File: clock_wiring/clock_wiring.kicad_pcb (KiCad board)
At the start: 2 copper layers, 142.2 x 142.2 mm, 38 parts, among them J1 Conn_01x01_Female, J2 Conn_01x01_Female, J3 Conn_01x01_Female, J4 Conn_01x01_Female, J5 Conn_01x01_Female, J6 Conn_01x01_Female, J8 Conn_01x01_Female, SW1 SW_Push, SW2 SW_Push, SW3 SW_Push, SW4 SW_Push, U1 ATmega328-P, U2 74HC595, U3 COM-09481, U4 AVR-ISP-6, U5 TinyRTC, Y1 Crystal

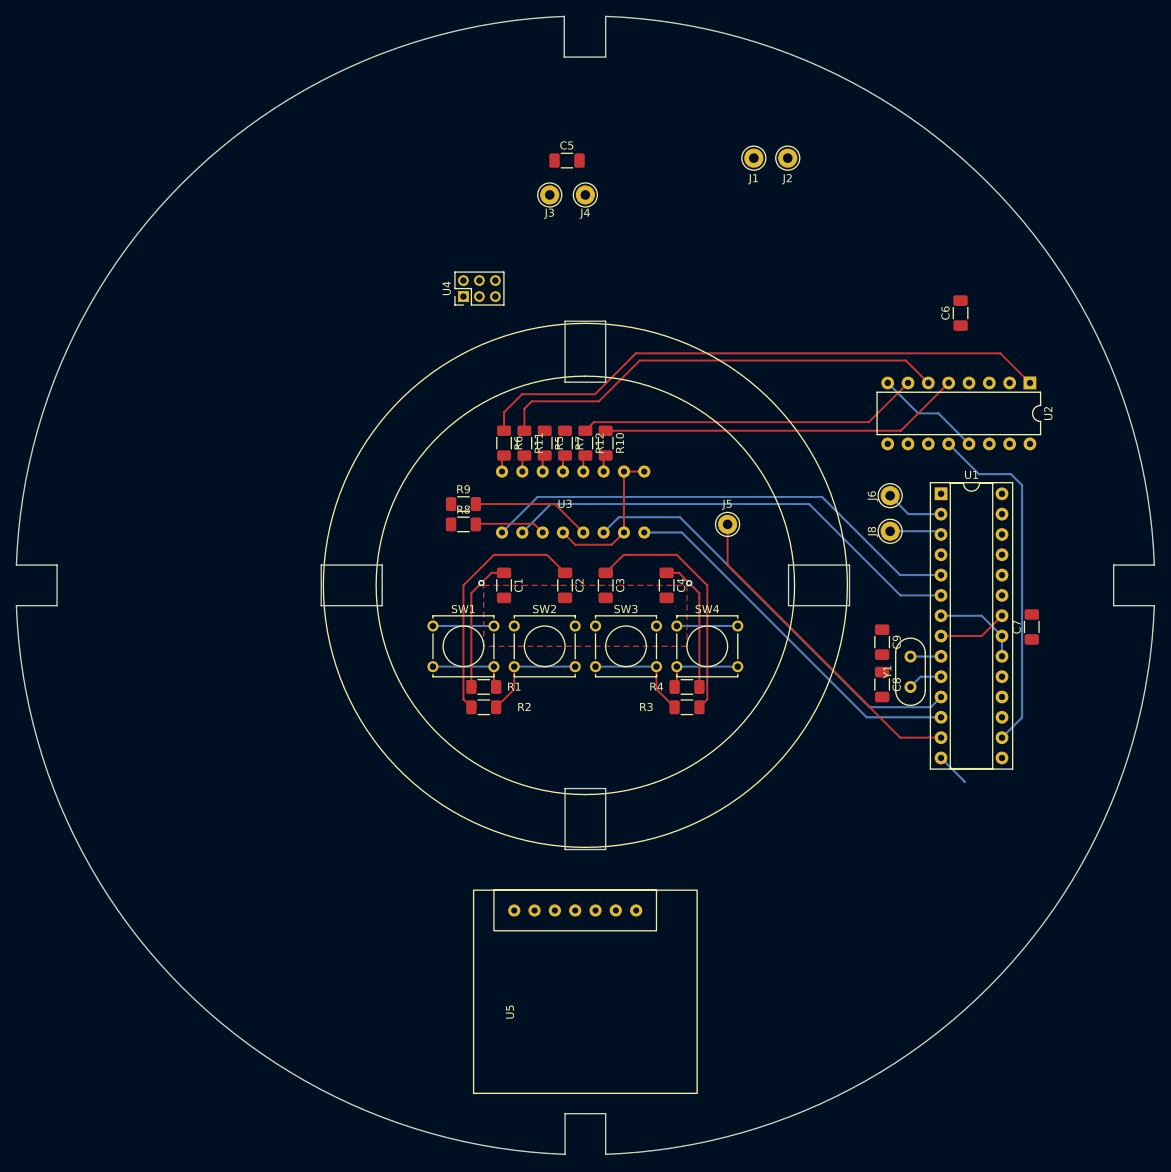
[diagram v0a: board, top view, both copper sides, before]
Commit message: Add traces for all signals, power on plane
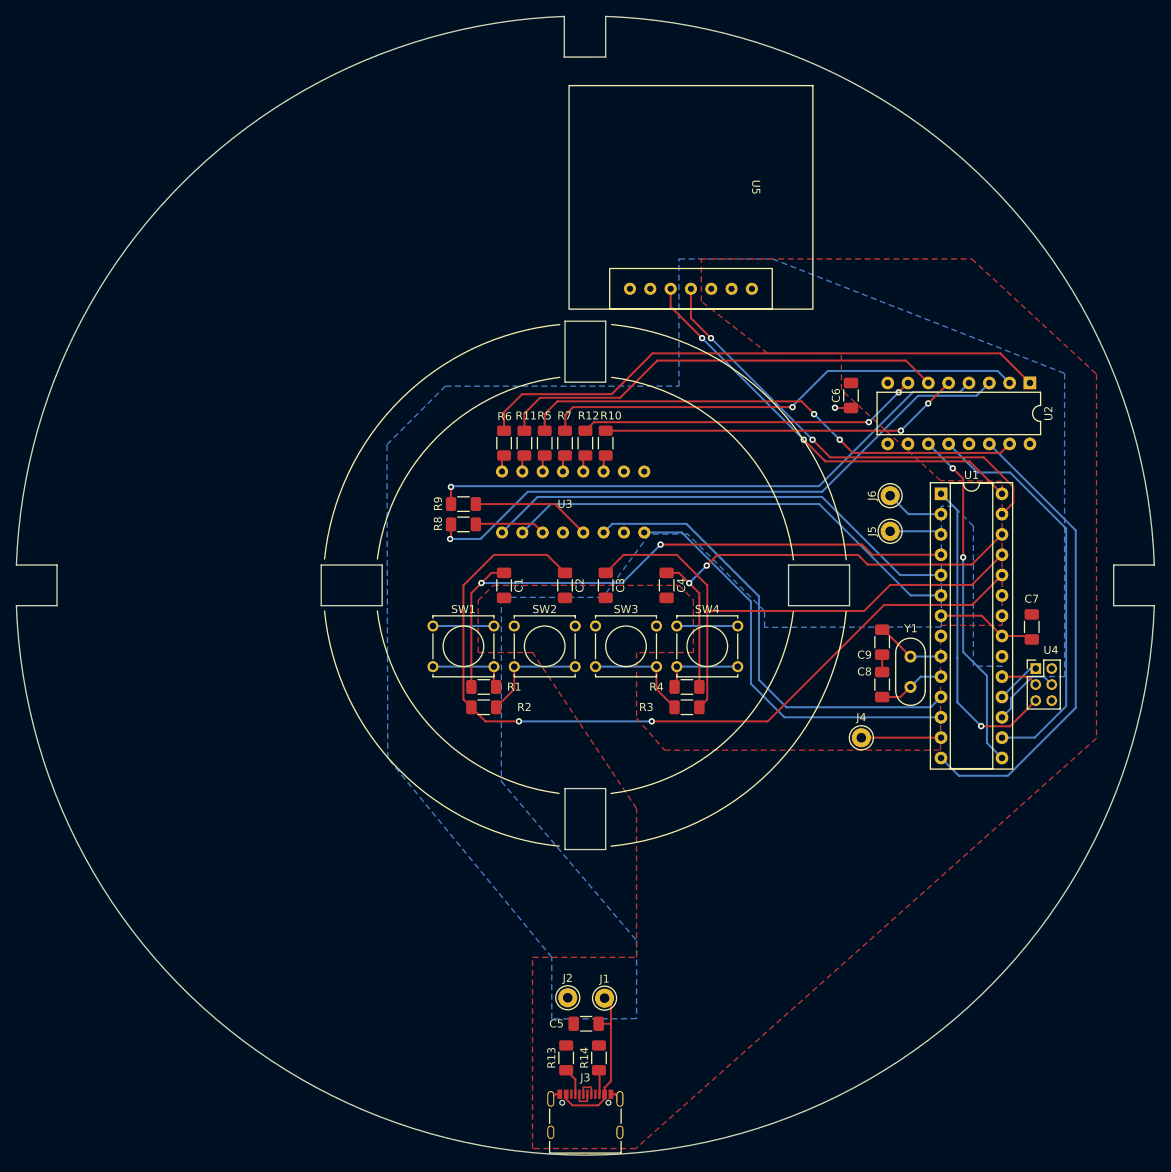
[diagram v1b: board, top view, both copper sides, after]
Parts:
- removed the J4 at (101.6, 52.8)
- added R13: 5.1k, Resistor_SMD:R_1206_3216Metric_Pad1.30x1.75mm_HandSolder, F.Cu at (99.2, 160.7)
- added R14: 5.1k, Resistor_SMD:R_1206_3216Metric_Pad1.30x1.75mm_HandSolder, F.Cu at (103.3, 160.7)
- J3: value Conn_01x01_Female -> USB_C_Receptacle_USB2.0; footprint Connector_Pin:Pin_D1.0mm_L10.0mm_LooseFit -> Connector_USB:USB_C_Receptacle_Palconn_UTC16-G
- moved J3 115.0 mm to (101.6, 167.7)
- moved J2 108.5 mm to (99.4, 153.2), turned to -90 degrees
- moved C5 107.9 mm to (101.7, 156.4), turned to 180 degrees
- moved U5 107.3 mm to (122.4, 51.8), turned to -90 degrees
- moved J1 106.6 mm to (104.0, 153.2), turned to -90 degrees
- moved U4 85.3 mm to (157.9, 112.0), turned to 0 degrees
- moved J4 31.5 mm to (136.1, 120.7)
- moved C6 17.1 mm to (134.8, 77.9)
- renumbered J5 to J4, J8 to J5
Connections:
- U5 pad 2: GND -> +5V
- U5 pad 3: +5V -> GND
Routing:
- net Net-(R8-Pad1): track 0.00 -> 77.3 mm, vias 0 -> 1
- net SET: track 31.1 -> 105.5 mm, vias 0 -> 2
- net Net-(R9-Pad1): track 0.00 -> 72.3 mm, vias 0 -> 1
- net Net-(R5-Pad1): track 0.00 -> 64.0 mm, vias 0 -> 2
- net Net-(R7-Pad1): track 0.00 -> 60.5 mm, vias 0 -> 1
- net MODE: track 17.2 -> 76.8 mm, vias 1 -> 2
- net SDA: track 0.00 -> 56.7 mm, vias 0 -> 2
- net BIT_OUT: track 4.24 -> 58.7 mm
- net SCL: track 0.00 -> 53.3 mm, vias 0 -> 2
- net CLK_OUT: track 0.00 -> 43.1 mm, vias 0 -> 2
- net DOWN: track 17.8 -> 59.5 mm, vias 1 -> 2
- net UP: track 30.9 -> 70.6 mm
- net RST: track 0.00 -> 39.3 mm, vias 0 -> 1
- net PXL_OUT: track 40.7 -> 9.97 mm
- net GND: track 37.5 -> 18.0 mm
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- added copper zone on B.Cu, net +5V
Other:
- board size 142.2 x 142.2 mm -> 142.2 x 142.3 mm

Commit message: update pcb ground plane(s), power trace, via/trace connections, fix pin sizes, notes in schematic on improvements to add
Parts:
- U4: footprint Connector_PinHeader_2.00mm:PinHeader_2x03_P2.00mm_Vertical -> Connector_PinHeader_2.54mm:PinHeader_2x03_P2.54mm_Vertical
- moved C6 25.9 mm to (159.1, 86.7), turned to 0 degrees
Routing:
- net +5V: track 35.4 -> 349.0 mm, vias 1 -> 0
- net LTCH_OUT: track 50.9 -> 53.4 mm
- net BIT_OUT: track 58.7 -> 60.7 mm
- net MOSI: track 9.50 -> 8.23 mm
- net SET: vias 2 -> 0
- net Net-(R12-Pad1): vias 2 -> 0
- net GND: vias 0 -> 67
- net CLK_OUT: vias 2 -> 0
- added copper zone on B.Cu, net GND
- removed copper zone on B.Cu, net +5V
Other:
- board text added: "LED Clock jenn-ylk V1.0 May 2023/May 2025/August 2026"
